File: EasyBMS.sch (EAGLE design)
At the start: 146 parts, among them Q10 BSS84LT1G, Q11 BSS84LT1G, Q12 BSS84LT1G, Q13 BSS84LT1G, Q2 BSS84LT1G, Q3 BSS84LT1G, Q4 BSS84LT1G, Q5 BSS84LT1G, Q6 BSS84LT1G, Q7 BSS84LT1G, Q8 BSS84LT1G, Q9 BSS84LT1G

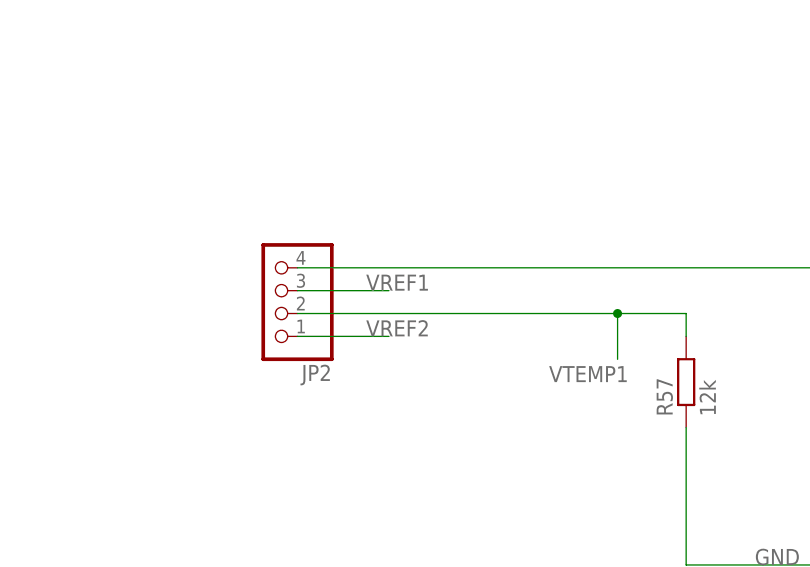
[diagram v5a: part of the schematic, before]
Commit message: VREF1 set to unused, only VREF2 is used now
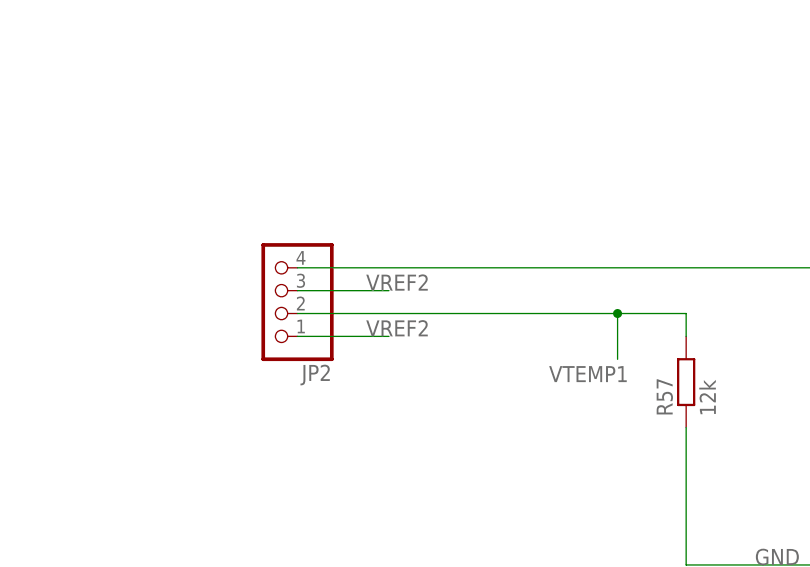
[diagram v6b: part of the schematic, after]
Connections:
- net VREF1: no longer JP2.3
- net VREF2: now also JP2.3
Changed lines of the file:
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@@
-</segment>
-<segment>
-<pinref part="JP2" gate="A" pin="3"/>
-<wire x1="-91.44" y1="208.28" x2="-81.28" y2="208.28" width="0.1524" layer="91"/>
-<label x="-83.82" y="208.28" size="1.778" layer="95"/>
 </segment>
 <segment>
@@
 <pinref part="JP5" gate="A" pin="14"/>
 </segment>
+<segment>
+<pinref part="JP2" gate="A" pin="3"/>
+<wire x1="-91.44" y1="208.28" x2="-81.28" y2="208.28" width="0.1524" layer="91"/>
+<label x="-83.82" y="208.28" size="1.778" layer="95"/>
+</segment>
 </net>

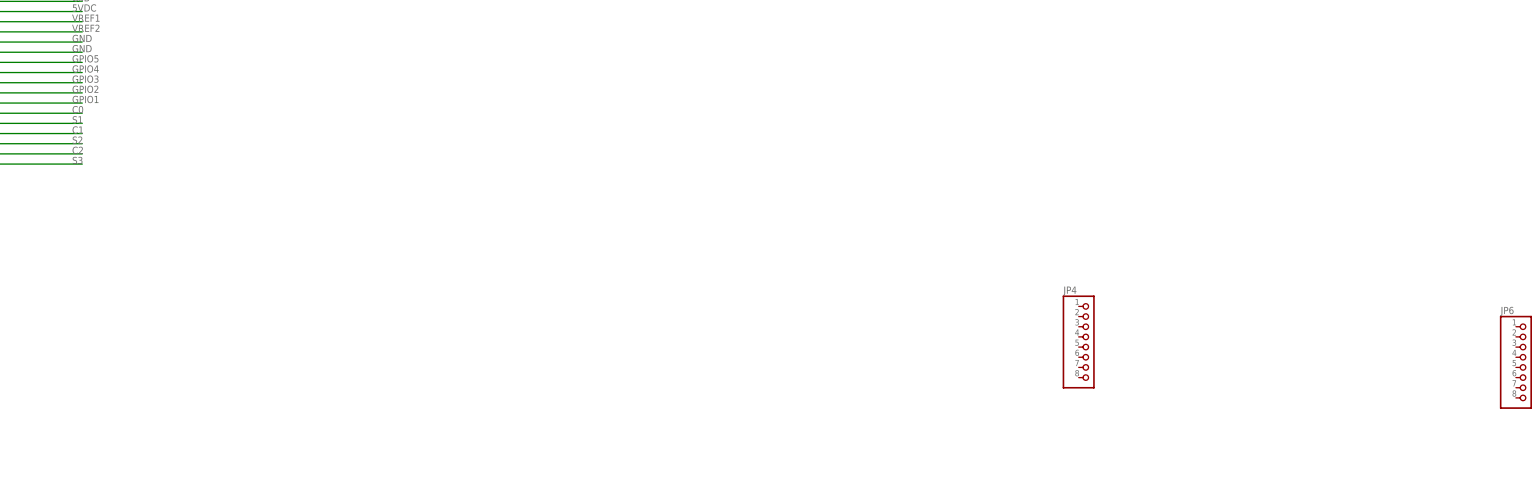
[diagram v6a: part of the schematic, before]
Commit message: restructured layout
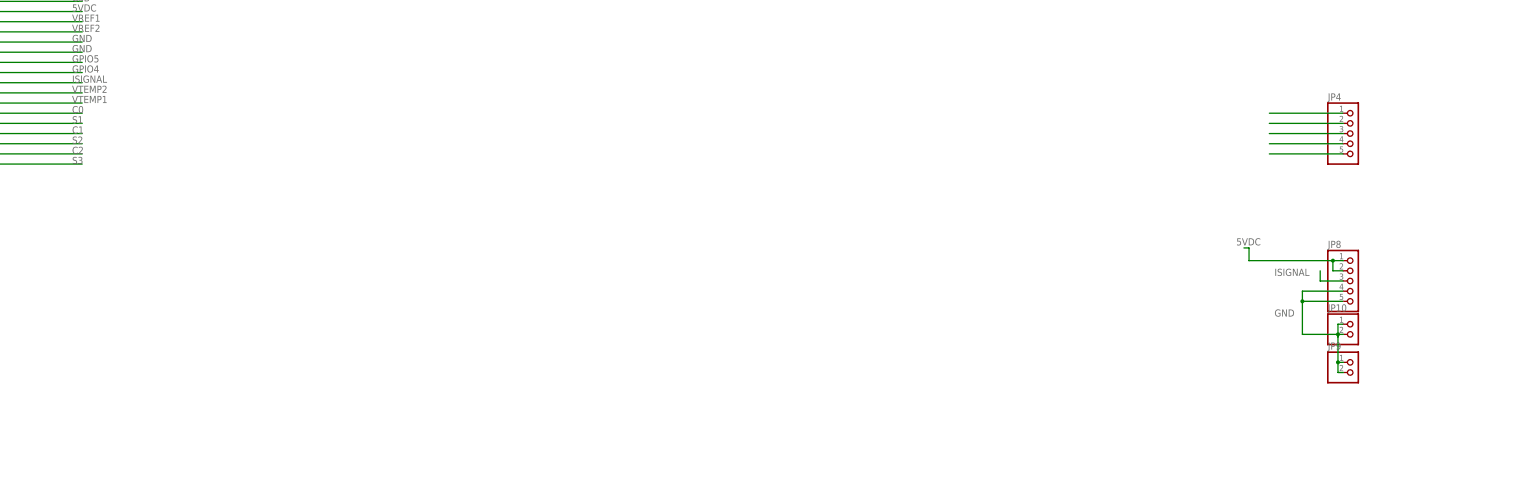
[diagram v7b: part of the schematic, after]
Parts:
- removed JP6: (no value), pinhead:PINHD-1X8
- added JP10, JP9: (no value), pinhead:PINHD-1X2
- added JP8: (no value), pinhead:PINHD-1X5
- JP4: device pinhead:PINHD-1X8 -> pinhead:PINHD-1X5
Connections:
- removed net GPIO2: JP5.26
- removed net GPIO3: JP5.24
- new net ISIGNAL: JP5.24, JP8.3
- new net N$15: JP4.2
- new net N$17: JP4.3
- new net N$18: JP4.4
- new net N$25: JP4.5
- new net N$7: JP4.1
- net 5VDC: now also JP8.1, JP8.2
- net GND: now also JP10.1, JP10.2, JP8.4, JP8.5, JP9.1, JP9.2
- net GPIO1: no longer JP5.28
- net VTEMP1: now also JP5.28
- net VTEMP2: now also JP5.26
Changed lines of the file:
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@@
 <setting verticaltext="up"/>
 </settings>
-<grid distance="0.1" unitdist="inch" unit="inch" style="lines" multiple="1" display="no" altdistance="0.01" altunitdist="inch" altunit="inch"/>
+<grid distance="25" unitdist="mil" unit="mil" style="lines" multiple="1" display="yes" altdistance="0.01" altunitdist="inch" altunit="inch"/>
 <layers>
 <layer number="1" name="Top" color="4" fill="1" visible="no" active="no"/>
@@
 <part name="C18" library="rcl" library_urn="urn:adsk.eagle:library:334" deviceset="C-EU" device="C1206" package3d_urn="urn:adsk.eagle:package:23618/2"/>
 <part name="C19" library="rcl" library_urn="urn:adsk.eagle:library:334" deviceset="C-EU" device="C1206" package3d_urn="urn:adsk.eagle:package:23618/2"/>
-<part name="JP4" library="pinhead" library_urn="urn:adsk.eagle:library:325" deviceset="PINHD-1X8" device="" package3d_urn="urn:adsk.eagle:package:22409/2"/>
-<part name="JP6" library="pinhead" library_urn="urn:adsk.eagle:library:325" deviceset="PINHD-1X8" device="" package3d_urn="urn:adsk.eagle:package:22409/2"/>
+<part name="JP8" library="pinhead" library_urn="urn:adsk.eagle:library:325" deviceset="PINHD-1X5" device="" package3d_urn="urn:adsk.eagle:package:22469/2"/>
+<part name="JP9" library="pinhead" library_urn="urn:adsk.eagle:library:325" deviceset="PINHD-1X2" device="" package3d_urn="urn:adsk.eagle:package:22435/2"/>
+<part name="JP10" library="pinhead" library_urn="urn:adsk.eagle:library:325" deviceset="PINHD-1X2" device="" package3d_urn="urn:adsk.eagle:package:22435/2"/>
+<part name="JP4" library="pinhead" library_urn="urn:adsk.eagle:library:325" deviceset="PINHD-1X5" device="" package3d_urn="urn:adsk.eagle:package:22469/2"/>
 </parts>
 <sheets>
@@
 <attribute name="VALUE" x="207.264" y="25.781" size="1.778" layer="96"/>
 </instance>
-<instance part="JP4" gate="A" x="462.28" y="248.92" smashed="yes">
-<attribute name="NAME" x="455.93" y="262.255" size="1.778" layer="95"/>
-<attribute name="VALUE" x="455.93" y="236.22" size="1.778" layer="96"/>
-</instance>
-<instance part="JP6" gate="A" x="571.5" y="243.84" smashed="yes">
-<attribute name="NAME" x="565.15" y="257.175" size="1.778" layer="95"/>
-<attribute name="VALUE" x="565.15" y="231.14" size="1.778" layer="96"/>
+<instance part="JP8" gate="A" x="528.32" y="265.43" smashed="yes">
+<attribute name="NAME" x="521.97" y="273.685" size="1.778" layer="95"/>
+<attribute name="VALUE" x="521.97" y="257.81" size="1.778" layer="96"/>
+</instance>
+<instance part="JP9" gate="G$1" x="528.32" y="242.57" smashed="yes">
+<attribute name="NAME" x="521.97" y="248.285" size="1.778" layer="95"/>
+<attribute name="VALUE" x="521.97" y="237.49" size="1.778" layer="96"/>
+</instance>
+<instance part="JP10" gate="G$1" x="528.32" y="252.095" smashed="yes">
+<attribute name="NAME" x="521.97" y="257.81" size="1.778" layer="95"/>
+<attribute name="VALUE" x="521.97" y="247.015" size="1.778" layer="96"/>
+</instance>
+<instance part="JP4" gate="A" x="528.32" y="302.26" smashed="yes">
+<attribute name="NAME" x="521.97" y="310.515" size="1.778" layer="95"/>
+<attribute name="VALUE" x="521.97" y="294.64" size="1.778" layer="96"/>
 </instance>
 </instances>
@@
 <wire x1="142.24" y1="332.74" x2="210.82" y2="332.74" width="0.1524" layer="91"/>
 <pinref part="JP5" gate="A" pin="10"/>
+</segment>
+<segment>
+<pinref part="JP8" gate="A" pin="1"/>
+<wire x1="525.78" y1="270.51" x2="523.24" y2="270.51" width="0.1524" layer="91"/>
+<pinref part="JP8" gate="A" pin="2"/>
+<wire x1="525.78" y1="267.97" x2="523.24" y2="267.97" width="0.1524" layer="91"/>
+<wire x1="523.24" y1="267.97" x2="523.24" y2="270.51" width="0.1524" layer="91"/>
+<wire x1="523.24" y1="270.51" x2="502.285" y2="270.51" width="0.1524" layer="91"/>
+<junction x="523.24" y="270.51"/>
+<wire x1="502.285" y1="270.51" x2="502.285" y2="273.685" width="0.1524" layer="91"/>
+<wire x1="502.285" y1="273.685" x2="501.015" y2="273.685" width="0.1524" layer="91"/>
+<label x="499.11" y="274.32" size="1.778" layer="95"/>
 </segment>
 </net>
@@
 <pinref part="JP5" gate="A" pin="18"/>
 </segment>
+<segment>
+<pinref part="JP9" gate="G$1" pin="2"/>
+<wire x1="524.51" y1="242.57" x2="525.78" y2="242.57" width="0.1524" layer="91"/>
+<pinref part="JP9" gate="G$1" pin="1"/>
+<wire x1="524.51" y1="245.11" x2="525.78" y2="245.11" width="0.1524" layer="91"/>
+<junction x="524.51" y="245.11"/>
+<wire x1="524.51" y1="245.11" x2="524.51" y2="242.57" width="0.1524" layer="91"/>
+<pinref part="JP10" gate="G$1" pin="2"/>
+<pinref part="JP10" gate="G$1" pin="1"/>
+<wire x1="524.51" y1="254.635" x2="525.78" y2="254.635" width="0.1524" layer="91"/>
+<wire x1="524.51" y1="254.635" x2="524.51" y2="252.095" width="0.1524" layer="91"/>
+<wire x1="524.51" y1="252.095" x2="525.78" y2="252.095" width="0.1524" layer="91"/>
+<junction x="524.51" y="252.095"/>
+<wire x1="524.51" y1="252.095" x2="524.51" y2="245.11" width="0.1524" layer="91"/>
+<wire x1="524.51" y1="252.095" x2="524.51" y2="251.46" width="0.1524" layer="91"/>
+<pinref part="JP8" gate="A" pin="5"/>
+<pinref part="JP8" gate="A" pin="4"/>
+<wire x1="525.78" y1="262.89" x2="515.62" y2="262.89" width="0.1524" layer="91"/>
+<wire x1="515.62" y1="262.89" x2="515.62" y2="260.35" width="0.1524" layer="91"/>
+<wire x1="515.62" y1="260.35" x2="525.78" y2="260.35" width="0.1524" layer="91"/>
+<wire x1="524.51" y1="252.095" x2="515.62" y2="252.095" width="0.1524" layer="91"/>
+<wire x1="515.62" y1="252.095" x2="515.62" y2="260.35" width="0.1524" layer="91"/>
+<junction x="515.62" y="260.35"/>
+<label x="508.635" y="256.54" size="1.778" layer="95"/>
+</segment>
 </net>
 <net name="N$202" class="0">
@@
 <junction x="-30.48" y="210.82"/>
 <label x="-25.4" y="208.28" size="1.778" layer="95"/>
+</segment>
+<segment>
+<label x="208.28" y="312.42" size="1.778" layer="95"/>
+<wire x1="210.82" y1="312.42" x2="142.24" y2="312.42" width="0.1524" layer="91"/>
+<pinref part="JP5" gate="A" pin="26"/>
 </segment>
 </net>
@@
 <junction x="-55.88" y="205.74"/>
 <label x="-63.5" y="198.12" size="1.778" layer="95"/>
+</segment>
+<segment>
+<label x="208.28" y="309.88" size="1.778" layer="95"/>
+<wire x1="142.24" y1="309.88" x2="210.82" y2="309.88" width="0.1524" layer="91"/>
+<pinref part="JP5" gate="A" pin="28"/>
 </segment>
 </net>
@@
 <junction x="370.84" y="93.98"/>
 </segment>
-<segment>
-<label x="208.28" y="309.88" size="1.778" layer="95"/>
-<wire x1="142.24" y1="309.88" x2="210.82" y2="309.88" width="0.1524" layer="91"/>
-<pinref part="JP5" gate="A" pin="28"/>
-</segment>
 </net>
 <net name="N$73" class="0">
@@
 </segment>
 </net>
-<net name="GPIO2" class="0">
-<segment>
-<label x="208.28" y="312.42" size="1.778" layer="95"/>
-<wire x1="210.82" y1="312.42" x2="142.24" y2="312.42" width="0.1524" layer="91"/>
-<pinref part="JP5" gate="A" pin="26"/>
-</segment>
-</net>
-<net name="GPIO3" class="0">
-<segment>
-<label x="208.28" y="314.96" size="1.778" layer="95"/>
-<wire x1="210.82" y1="314.96" x2="142.24" y2="314.96" width="0.1524" layer="91"/>
-<pinref part="JP5" gate="A" pin="24"/>
-</segment>
-</net>
 <net name="GPIO4" class="0">
 <segment>
@@
 </segment>
 </net>
+<net name="ISIGNAL" class="0">
+<segment>
+<pinref part="JP8" gate="A" pin="3"/>
+<wire x1="525.78" y1="265.43" x2="520.065" y2="265.43" width="0.1524" layer="91"/>
+<wire x1="520.065" y1="265.43" x2="520.065" y2="267.97" width="0.1524" layer="91"/>
+<label x="508.635" y="266.7" size="1.778" layer="95"/>
+</segment>
+<segment>
+<label x="208.28" y="314.96" size="1.778" layer="95"/>
+<wire x1="210.82" y1="314.96" x2="142.24" y2="314.96" width="0.1524" layer="91"/>
+<pinref part="JP5" gate="A" pin="24"/>
+</segment>
+</net>
+<net name="N$7" class="0">
+<segment>
+<pinref part="JP4" gate="A" pin="1"/>
+<wire x1="525.78" y1="307.34" x2="507.365" y2="307.34" width="0.1524" layer="91"/>
+</segment>
+</net>
+<net name="N$15" class="0">
+<segment>
+<pinref part="JP4" gate="A" pin="2"/>
+<wire x1="525.78" y1="304.8" x2="507.365" y2="304.8" width="0.1524" layer="91"/>
+</segment>
+</net>
+<net name="N$17" class="0">
+<segment>
+<pinref part="JP4" gate="A" pin="3"/>
+<wire x1="525.78" y1="302.26" x2="507.365" y2="302.26" width="0.1524" layer="91"/>
+</segment>
+</net>
+<net name="N$18" class="0">
+<segment>
+<pinref part="JP4" gate="A" pin="4"/>
+<wire x1="525.78" y1="299.72" x2="507.365" y2="299.72" width="0.1524" layer="91"/>
+</segment>
+</net>
+<net name="N$25" class="0">
+<segment>
+<pinref part="JP4" gate="A" pin="5"/>
+<wire x1="525.78" y1="297.18" x2="507.365" y2="297.18" width="0.1524" layer="91"/>
+</segment>
+</net>
